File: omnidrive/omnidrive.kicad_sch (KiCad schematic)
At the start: 85 parts, among them J1 AudioJack3, J6 AudioJack2, U1 TL072, U2 TL072

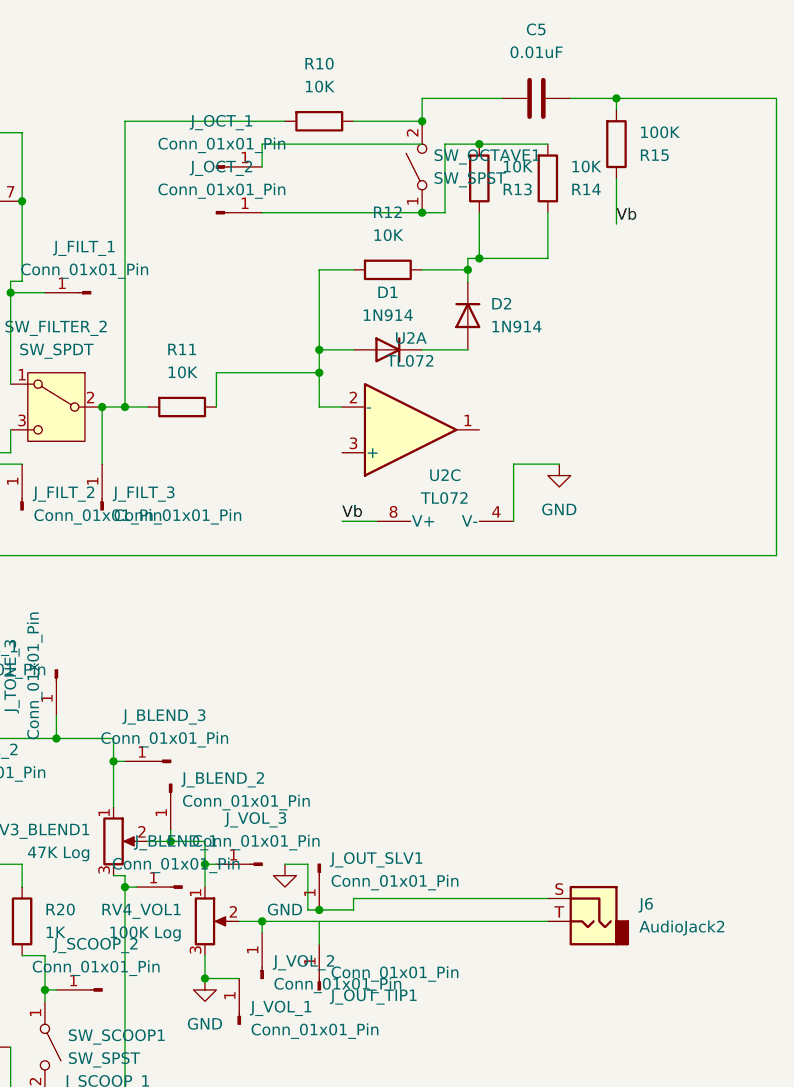
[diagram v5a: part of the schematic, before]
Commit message: fix some cnxs and place everything
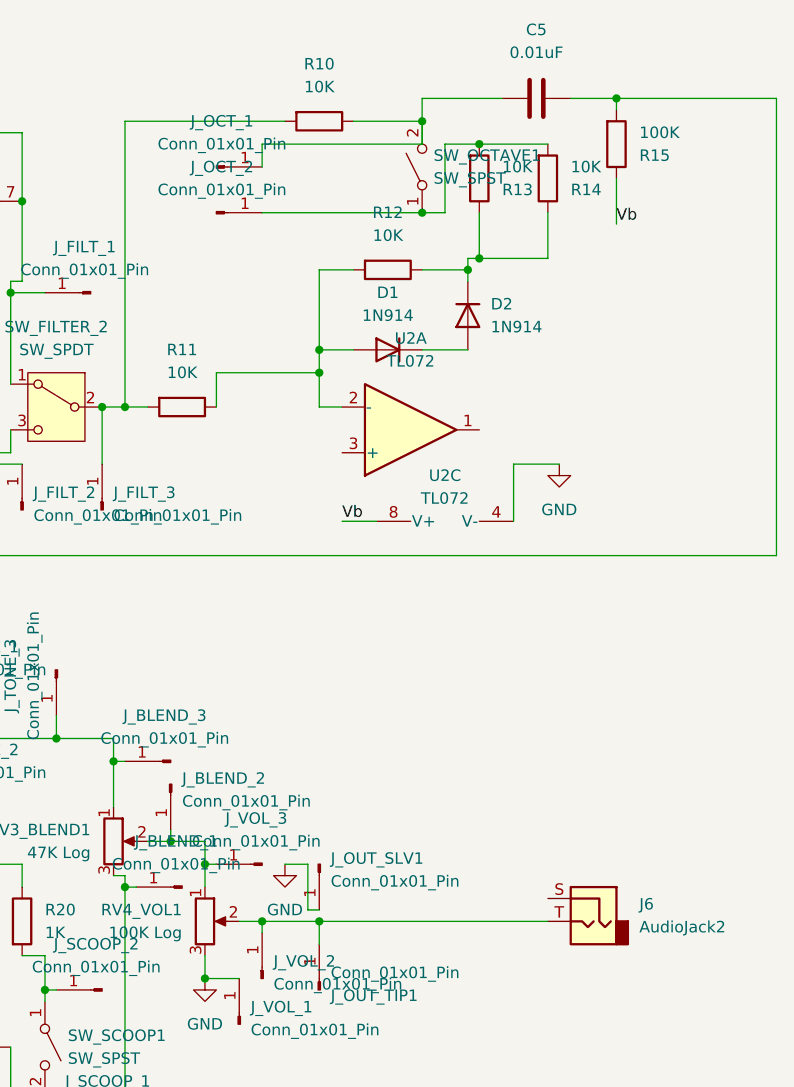
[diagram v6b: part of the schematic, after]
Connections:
- net GND: no longer J6.S
- net at C5.1, R10.1, SW_OCTAVE1.2 (B): now also J_OCT_1.1 (Pin_1)
- net at J6.T, J_VOL_2.1 (Pin_1), RV4_VOL1.2: now also J_OUT_TIP1.1 (Pin_1)

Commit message: some routing but not complete
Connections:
- net +9V: now also U2.8 (V+)
- net Vb: now also U2.3 (+); no longer U2.8 (V+)
- net at D1.1 (K), D2.2 (A): now also U2.1
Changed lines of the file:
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@@
   (junction (at 71.12 30.48) (diameter 0) (color 0 0 0 0)
   )
+  (junction (at 218.44 44.45) (diameter 0) (color 0 0 0 0)
+  )
   (junction (at 161.29 82.55) (diameter 0) (color 0 0 0 0)
   )
@@
     (stroke (width 0) (type default))
   )
-  (wire (pts (xy 215.9 44.45) (xy 220.98 44.45))
+  (wire (pts (xy 215.9 44.45) (xy 218.44 44.45))
     (stroke (width 0) (type default))
   )
@@
     (stroke (width 0) (type default))
   )
-  (wire (pts (xy 207.01 63.5) (xy 210.82 63.5))
-    (stroke (width 0) (type default))
-  )
   (wire (pts (xy 226.06 57.15) (xy 226.06 63.5))
     (stroke (width 0) (type default))
@@
     (stroke (width 0) (type default))
   )
+  (wire (pts (xy 218.44 44.45) (xy 220.98 44.45))
+    (stroke (width 0) (type default))
+  )
   (wire (pts (xy 144.78 86.36) (xy 144.78 80.01))
     (stroke (width 0) (type default))
@@
     (stroke (width 0) (type default))
   )
+  (wire (pts (xy 218.44 46.99) (xy 218.44 44.45))
+    (stroke (width 0) (type default))
+  )
   (wire (pts (xy 215.9 21.59) (xy 198.12 21.59))
     (stroke (width 0) (type default))
@@
     (stroke (width 0) (type default))
   )
+  (wire (pts (xy 204.47 55.88) (xy 207.01 55.88))
+    (stroke (width 0) (type default))
+  )
   (wire (pts (xy 80.01 36.83) (xy 85.09 36.83))
     (stroke (width 0) (type default))
@@
     (stroke (width 0) (type default))
   )
+  (wire (pts (xy 222.25 53.34) (xy 222.25 46.99))
+    (stroke (width 0) (type default))
+  )
   (wire (pts (xy 161.29 91.44) (xy 161.29 93.98))
     (stroke (width 0) (type default))
@@
     (stroke (width 0) (type default))
   )
+  (wire (pts (xy 208.28 63.5) (xy 210.82 63.5))
+    (stroke (width 0) (type default))
+  )
   (wire (pts (xy 175.26 85.09) (xy 175.26 87.63))
     (stroke (width 0) (type default))
@@
   )
   (wire (pts (xy 170.18 48.26) (xy 170.18 38.1))
+    (stroke (width 0) (type default))
+  )
+  (wire (pts (xy 222.25 46.99) (xy 218.44 46.99))
     (stroke (width 0) (type default))
   )
@@
     (effects (font (size 1.27 1.27)) (justify left bottom))
   )
+  (label "+9V" (at 208.28 63.5 0) (fields_autoplaced)
+    (effects (font (size 1.27 1.27)) (justify left bottom))
+  )
   (label "Vb" (at 67.31 73.66 0) (fields_autoplaced)
     (effects (font (size 1.27 1.27)) (justify left bottom))
   )
+  (label "Vb" (at 204.47 55.88 0) (fields_autoplaced)
+    (effects (font (size 1.27 1.27)) (justify left bottom))
+  )
   (label "Vb" (at 237.49 30.48 0) (fields_autoplaced)
     (effects (font (size 1.27 1.27)) (justify left bottom))
@@
     (effects (font (size 1.27 1.27)) (justify left bottom))
   )
-  (label "Vb" (at 207.01 63.5 0) (fields_autoplaced)
-    (effects (font (size 1.27 1.27)) (justify left bottom))
-  )
